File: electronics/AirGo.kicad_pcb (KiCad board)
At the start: 2 copper layers, 61 x 55.9 mm, 6 parts, among them J1 Power Connector, J2 FTDI Connector, J3 Motor Connector, J4 Button, U2 DRV8838, U3 ARDUINO_PRO_MINI

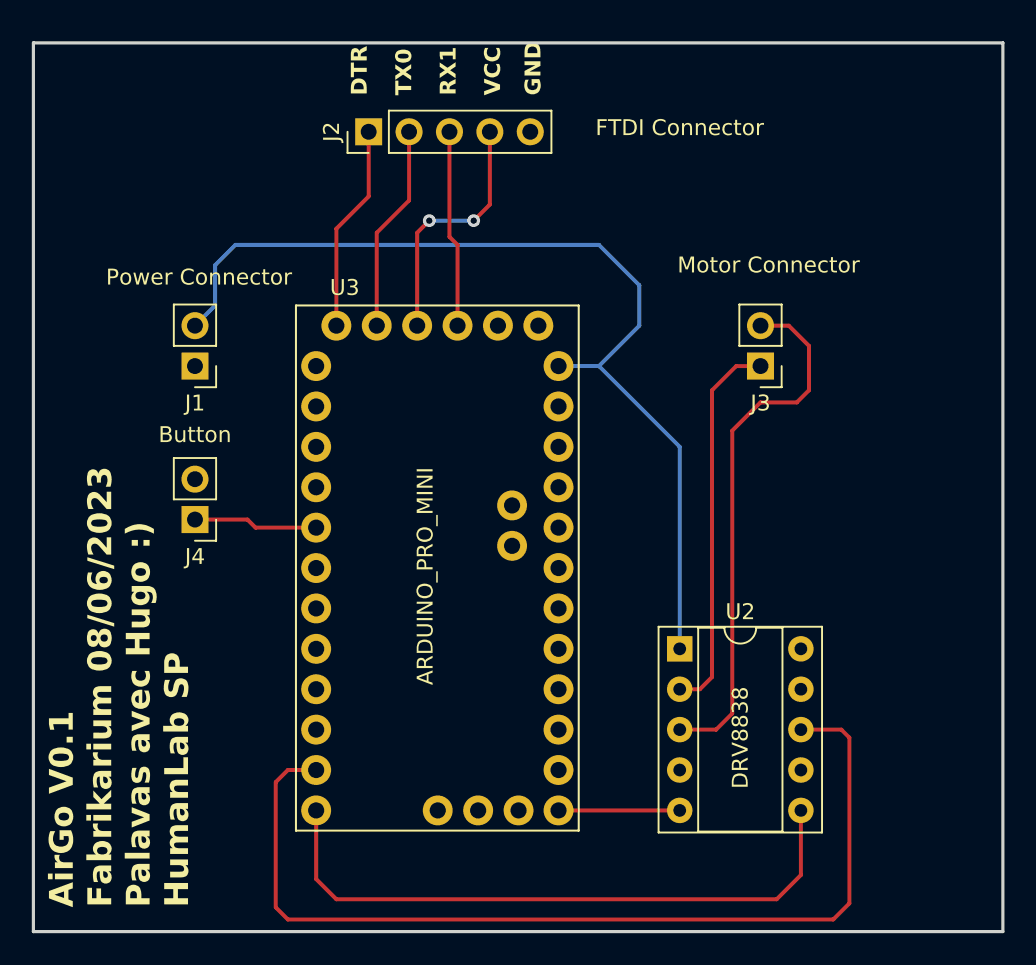
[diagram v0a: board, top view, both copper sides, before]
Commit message: Fix pcb (edited with Kicad 8.0) and generate gerber & drill files
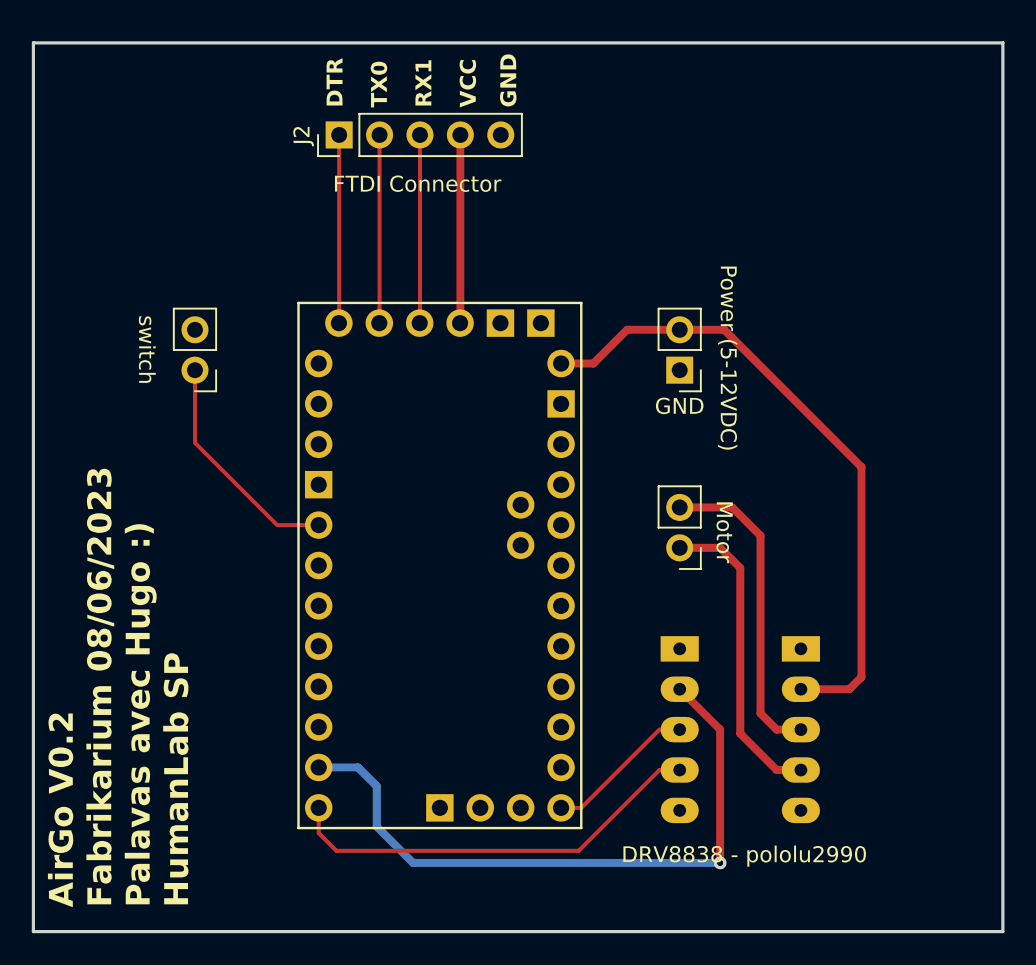
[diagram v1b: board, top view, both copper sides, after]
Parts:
- removed U3: ARDUINO_PRO_MINI, ARDUINO_PRO_MINI:MODULE_ARDUINO_PRO_MINI
- added A1: Clone_Pro_Mini_Socket, PCM_arduino-library:Clone_Pro_Mini_Socket, F.Cu at (117.0, 73.5)
- J1: value Power Connector -> Screw_Terminal_01x02
- J2: value FTDI Connector -> Conn_01x05_Socket
- J3: renamed from J4; value Button -> Screw_Terminal_01x02
- J4: renamed from J3; value Motor Connector -> Screw_Terminal_01x02
- U2: value DRV8838 -> DRV8838 - pololu2990; footprint Package_DIP:DIP-10_W7.62mm_Socket -> Package_DIP:DIP-10_W7.62mm_LongPads
- moved J1 30.5 mm to (132.1, 61.2)
- moved J4 12.5 mm to (132.1, 72.4)
- moved J3 9.39 mm to (101.6, 61.2)
- moved J2 1.87 mm to (110.7, 46.4)
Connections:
- J1 pad 2: Net-(J1-Pin_2) -> /VIN
- J4 pad 1: Net-(J3-Pin_1) -> /OUT1
- J4 pad 2: Net-(J3-Pin_2) -> /OUT2
- U2 pad 1: Net-(J1-Pin_2) -> GND
- U2 pad 10: (no net) -> GND
- U2 pad 2: Net-(J3-Pin_1) -> /VCC_DRV
- U2 pad 3: Net-(J3-Pin_2) -> /EN
- U2 pad 4: GND -> /PH
- U2 pad 5: Net-(U2-EN) -> unconnected-(U2-~{SLEEP}-Pad5)
- U2 pad 6: Net-(U2-PH) -> unconnected-(U2-VM-Pad6)
- U2 pad 7: unconnected-(U2-~{SLEEP}-Pad7) -> /OUT1
- U2 pad 8: Net-(U2-VCC) -> /OUT2
- U2 pad 9: GND -> /VIN
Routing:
- net Net-(U2-VCC): track 61.2 -> 0.00 mm
- net Net-(J1-Pin_2): track 61.1 -> 0.00 mm
- net /VCC_DRV: track 0.00 -> 41.2 mm, vias 0 -> 1
- net /VIN: track 0.00 -> 40.7 mm
- net Net-(U2-PH): track 40.0 -> 0.00 mm
- net Net-(J3-Pin_2): track 33.7 -> 0.00 mm
- net /PH: track 0.00 -> 26.9 mm
- net Net-(J3-Pin_1): track 24.1 -> 0.00 mm
- net /OUT2: track 0.00 -> 20.0 mm
- net /OUT1: track 0.00 -> 19.5 mm
- net /EN: track 0.00 -> 9.50 mm
- net Net-(U2-EN): track 7.62 -> 0.00 mm
- net Net-(A1-D2_INT0): track 7.83 -> 14.5 mm
- net Net-(J2-Pin_4): track 15.7 -> 11.8 mm, vias 2 -> 0
- net Net-(A1-~{DTR}): track 13.0 -> 11.8 mm
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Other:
- board text added: "AirGo V0.2 Fabrikarium 08/06/2023 Palavas avec Hugo :) HumanLab SP"
- board text removed: "AirGo V0.1 Fabrikarium 08/06/2023 Palavas avec Hugo :) HumanLab SP"
